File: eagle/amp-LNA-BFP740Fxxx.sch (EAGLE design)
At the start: 22 parts, among them J1 142-0701-851, J2 142-0701-851, Q1 PMOS, Q2 BFP740F

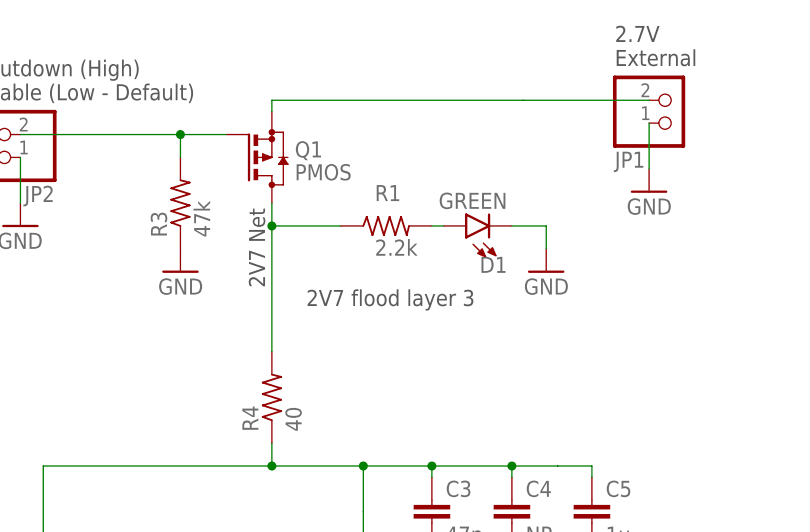
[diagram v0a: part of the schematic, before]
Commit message: BFP740F update value
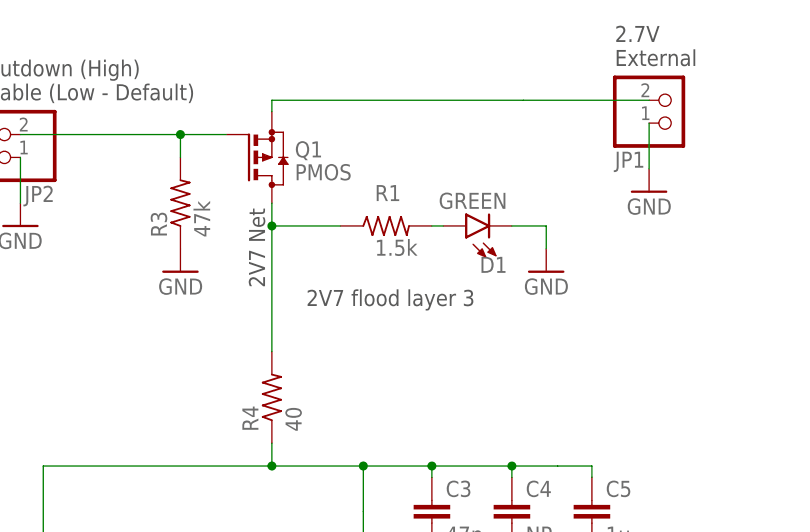
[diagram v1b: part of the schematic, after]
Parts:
- R1: value 2.2k -> 1.5k
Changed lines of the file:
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@@
 </part>
 <part name="GND80" library="supply1" deviceset="GND" device=""/>
-<part name="R1" library="oresat-rcl" deviceset="R-US_" device="0603-B-NOSILK" value="2.2k"/>
+<part name="R1" library="oresat-rcl" deviceset="R-US_" device="0603-B-NOSILK" value="1.5k"/>
 <part name="J1" library="J-Cinch-142-0701-851-SMA-end-launch" deviceset="142-0701-851" device=""/>
 <part name="J2" library="J-Cinch-142-0701-851-SMA-end-launch" deviceset="142-0701-851" device=""/>

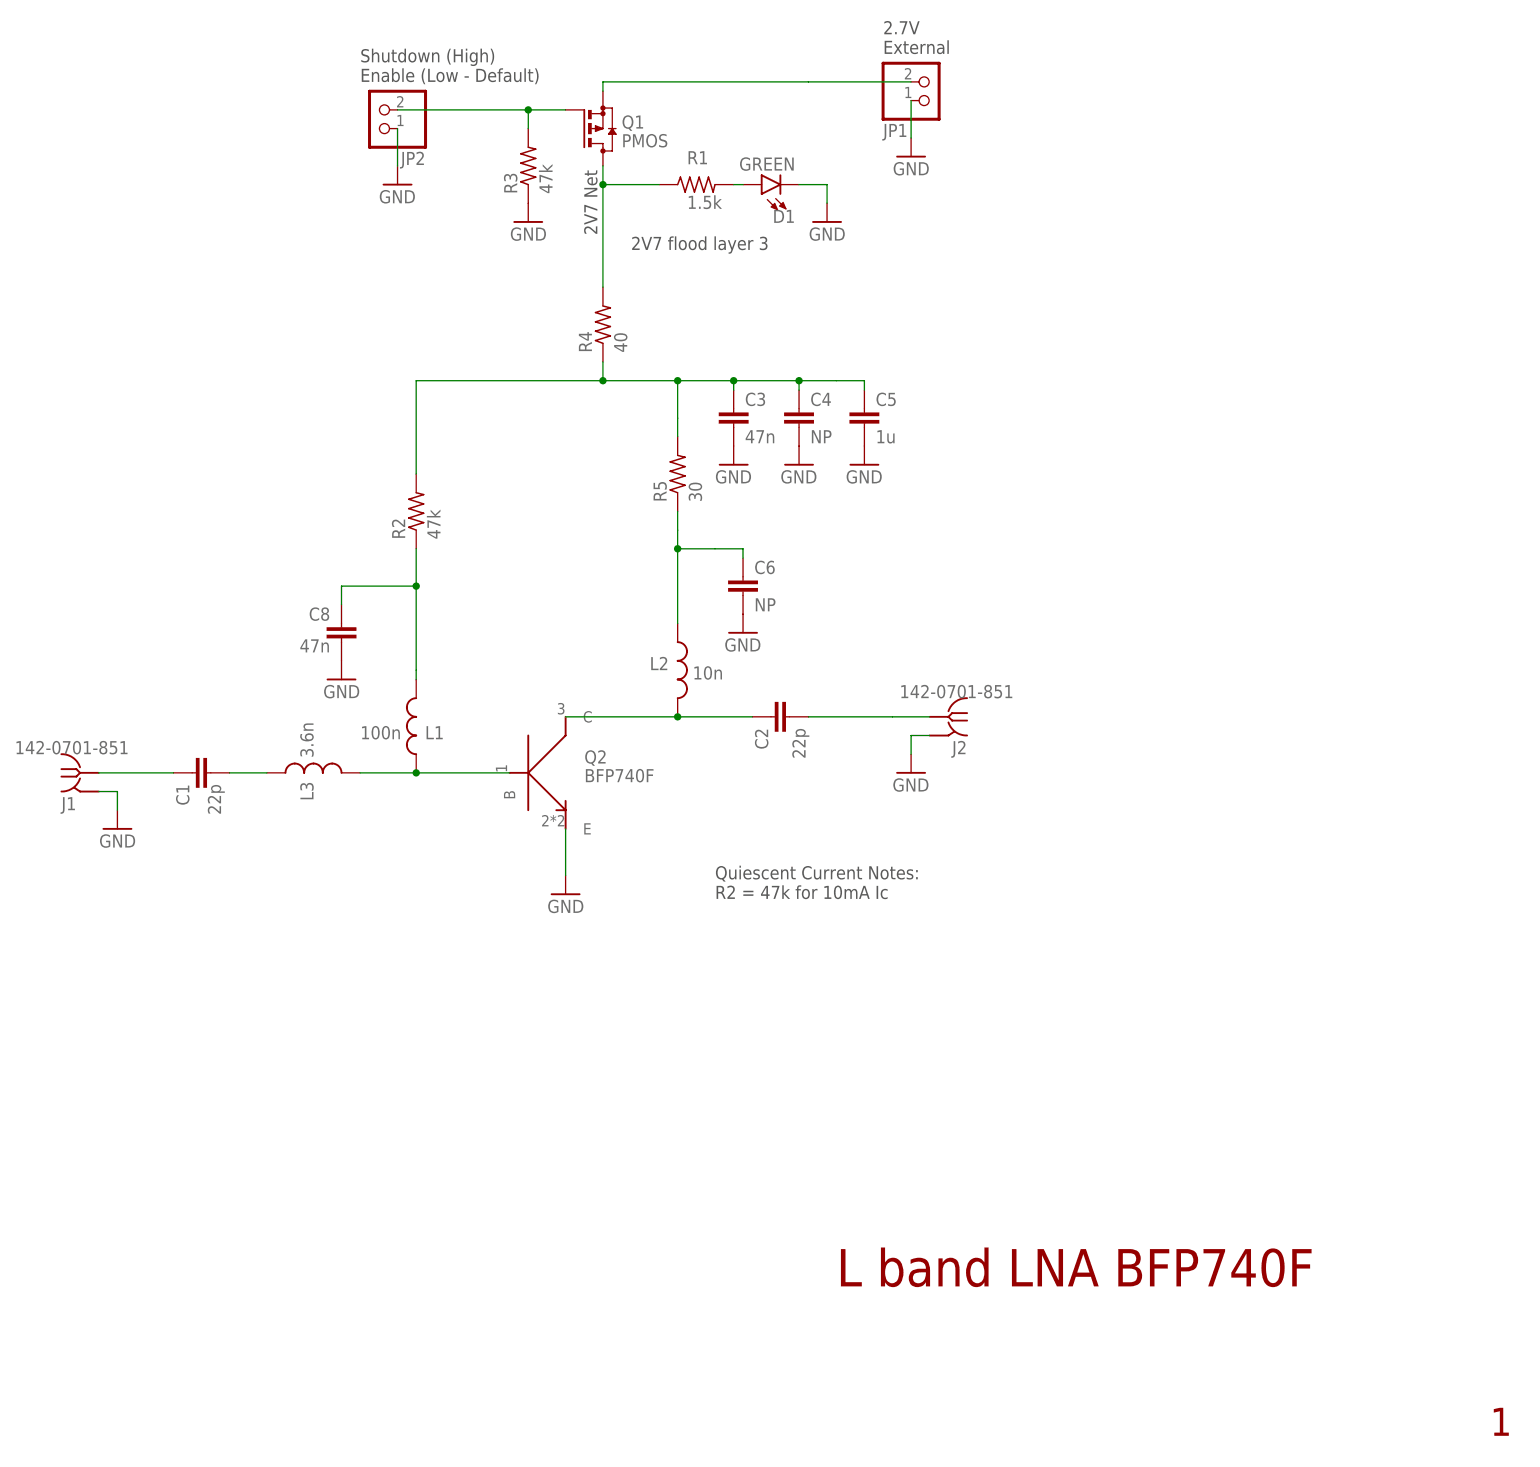
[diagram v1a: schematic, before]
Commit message: Add initial layout for LNA BFP740F
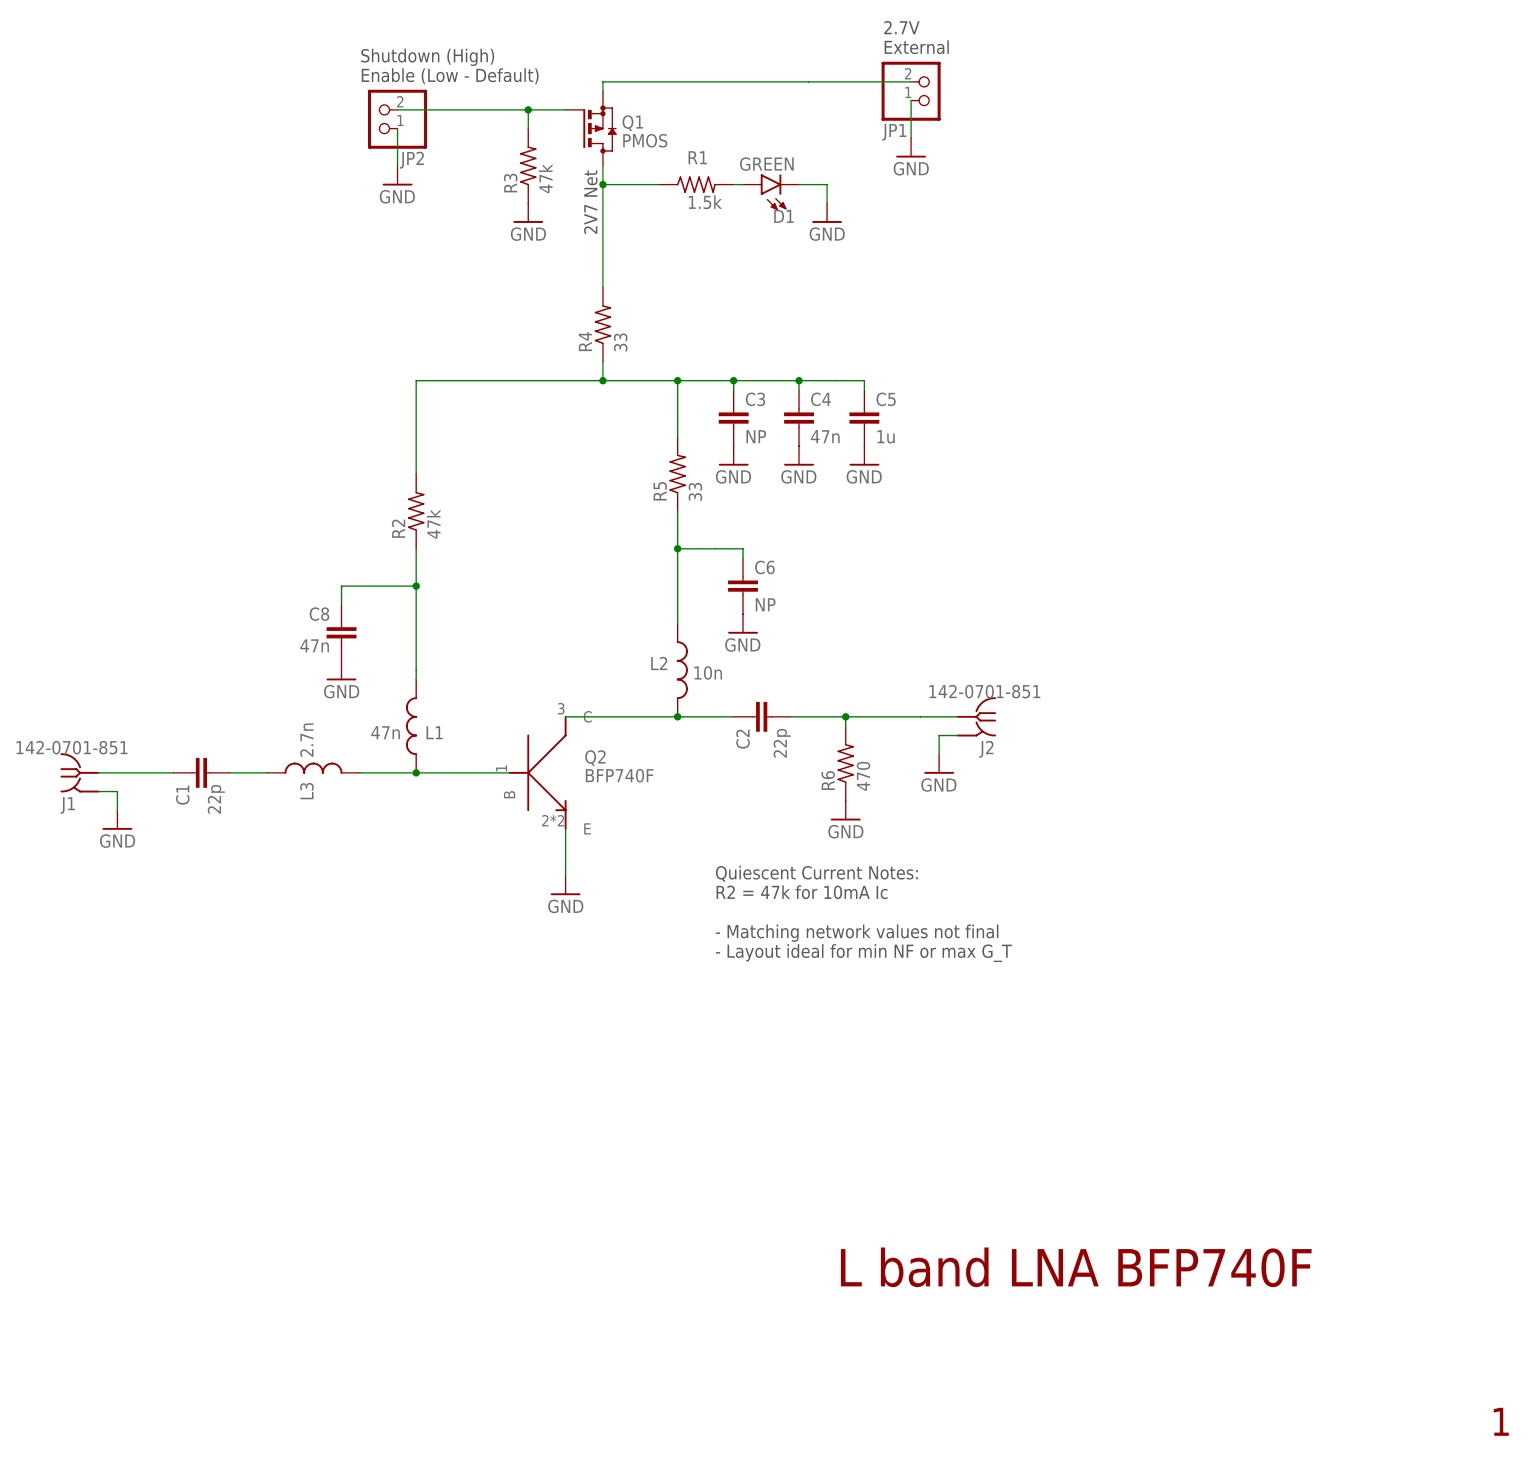
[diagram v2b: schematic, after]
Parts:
- added R6: 470, oresat-rcl:R-US_0603-C-NOSILK
- C3: value 47n -> NP; device oresat-rcl:C-EU0603-B-NOSILK -> oresat-rcl:C-EU0603-C-NOSILK
- C4: value NP -> 47n; device oresat-rcl:C-EU0603-B-NOSILK -> oresat-rcl:C-EU0603-C-NOSILK
- C5, C8: device oresat-rcl:C-EU0603-B-NOSILK -> oresat-rcl:C-EU0603-C-NOSILK
- C6: device oresat-rcl:C-EU0402-C-NOSILK -> oresat-rcl:C-EU0402-B-NOSILK
- L1: value 100n -> 47n
- L2: device oresat-rcl:L-US0402-C-NOSILK -> oresat-rcl:L-US0603-C-NOSILK
- L3: value 3.6n -> 2.7n
- R1, R2: device oresat-rcl:R-US_0603-B-NOSILK -> oresat-rcl:R-US_0603-C-NOSILK
- R4: value 40 -> 33; device oresat-rcl:R-US_0603-B-NOSILK -> oresat-rcl:R-US_0603-C-NOSILK
- R5: value 30 -> 33; device oresat-rcl:R-US_0603-B-NOSILK -> oresat-rcl:R-US_0603-C-NOSILK
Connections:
- net N$11 renamed B
- net N$4 renamed C
- net RF-IN renamed RF_IN
- removed net N$5: Q1.D, R1.1, R4.2
- new net CAPS: C3.1, C4.1, C5.1, R2.2, R4.1, R5.2
- net 2V7: now also Q1.D, R1.1, R4.2; no longer C3.1, C4.1, C5.1, R2.2, R4.1, R5.2
- net GND: now also R6.1
- net RF_OUT: now also R6.2
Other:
- note added: "Quiescent Current Notes: R2 = 47k for 10mA Ic - Matching network values not final - Layout ideal for min NF or max G_T"
- note removed: "2V7 flood layer 3"
- note removed: "Quiescent Current Notes: R2 = 47k for 10mA Ic"
- moved on the sheet: C2, J2
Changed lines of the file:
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@@
 <part name="GND29" library="supply1" library_urn="urn:adsk.eagle:library:371" deviceset="GND" device=""/>
 <part name="GND30" library="supply1" library_urn="urn:adsk.eagle:library:371" deviceset="GND" device=""/>
-<part name="C5" library="oresat-rcl" deviceset="C-EU" device="0603-B-NOSILK" value="1u"/>
-<part name="C4" library="oresat-rcl" deviceset="C-EU" device="0603-B-NOSILK" value="NP"/>
-<part name="C3" library="oresat-rcl" deviceset="C-EU" device="0603-B-NOSILK" value="47n"/>
+<part name="C5" library="oresat-rcl" deviceset="C-EU" device="0603-C-NOSILK" value="1u"/>
+<part name="C4" library="oresat-rcl" deviceset="C-EU" device="0603-C-NOSILK" value="47n"/>
+<part name="C3" library="oresat-rcl" deviceset="C-EU" device="0603-C-NOSILK" value="NP"/>
 <part name="JP1" library="pinhead" library_urn="urn:adsk.eagle:library:325" deviceset="PINHD-1X2" device="" package3d_urn="urn:adsk.eagle:package:22435/2"/>
 <part name="GND4" library="supply1" library_urn="urn:adsk.eagle:library:371" deviceset="GND" device=""/>
@@
 </part>
 <part name="GND80" library="supply1" deviceset="GND" device=""/>
-<part name="R1" library="oresat-rcl" deviceset="R-US_" device="0603-B-NOSILK" value="1.5k"/>
+<part name="R1" library="oresat-rcl" deviceset="R-US_" device="0603-C-NOSILK" value="1.5k"/>
 <part name="J1" library="J-Cinch-142-0701-851-SMA-end-launch" deviceset="142-0701-851" device=""/>
 <part name="J2" library="J-Cinch-142-0701-851-SMA-end-launch" deviceset="142-0701-851" device=""/>
 <part name="C1" library="oresat-rcl" deviceset="C-EU" device="0402-C-NOSILK" value="22p"/>
-<part name="L1" library="oresat-rcl" deviceset="L-US" device="0603-C-NOSILK" value="100n"/>
+<part name="L1" library="oresat-rcl" deviceset="L-US" device="0603-C-NOSILK" value="47n"/>
 <part name="GND5" library="supply1" library_urn="urn:adsk.eagle:library:371" deviceset="GND" device=""/>
 <part name="GND7" library="supply1" library_urn="urn:adsk.eagle:library:371" deviceset="GND" device=""/>
 <part name="GND8" library="supply1" library_urn="urn:adsk.eagle:library:371" deviceset="GND" device=""/>
-<part name="C8" library="oresat-rcl" deviceset="C-EU" device="0603-B-NOSILK" value="47n"/>
+<part name="C8" library="oresat-rcl" deviceset="C-EU" device="0603-C-NOSILK" value="47n"/>
 <part name="Q1" library="transistor-small-signal" library_urn="urn:adsk.eagle:library:401" deviceset="BSS84" device="" package3d_urn="urn:adsk.eagle:package:28738/2" value="PMOS"/>
 <part name="JP2" library="pinhead" library_urn="urn:adsk.eagle:library:325" deviceset="PINHD-1X2" device="" package3d_urn="urn:adsk.eagle:package:22435/2"/>
@@
 <part name="R3" library="oresat-rcl" deviceset="R-US_" device="0402-B-NOSILK" value="47k"/>
 <part name="GND3" library="supply1" library_urn="urn:adsk.eagle:library:371" deviceset="GND" device=""/>
-<part name="R5" library="oresat-rcl" deviceset="R-US_" device="0603-B-NOSILK" value="30"/>
+<part name="R5" library="oresat-rcl" deviceset="R-US_" device="0603-C-NOSILK" value="33"/>
 <part name="GND2" library="supply1" library_urn="urn:adsk.eagle:library:371" deviceset="GND" device=""/>
 <part name="Q2" library="Q-Infineon-BFPXXX-RF-BJT" deviceset="BFPXXXF" device="" value="BFP740F"/>
-<part name="C6" library="oresat-rcl" deviceset="C-EU" device="0402-C-NOSILK" value="NP"/>
+<part name="C6" library="oresat-rcl" deviceset="C-EU" device="0402-B-NOSILK" value="NP"/>
 <part name="GND6" library="supply1" library_urn="urn:adsk.eagle:library:371" deviceset="GND" device=""/>
-<part name="R2" library="oresat-rcl" deviceset="R-US_" device="0603-B-NOSILK" value="47k"/>
-<part name="L3" library="oresat-rcl" deviceset="L-US" device="0402-C-NOSILK" value="3.6n"/>
-<part name="R4" library="oresat-rcl" deviceset="R-US_" device="0603-B-NOSILK" value="40"/>
-<part name="L2" library="oresat-rcl" deviceset="L-US" device="0402-C-NOSILK" value="10n"/>
+<part name="R2" library="oresat-rcl" deviceset="R-US_" device="0603-C-NOSILK" value="47k"/>
+<part name="L3" library="oresat-rcl" deviceset="L-US" device="0402-C-NOSILK" value="2.7n"/>
+<part name="R4" library="oresat-rcl" deviceset="R-US_" device="0603-C-NOSILK" value="33"/>
+<part name="L2" library="oresat-rcl" deviceset="L-US" device="0603-C-NOSILK" value="10n"/>
+<part name="GND9" library="supply1" library_urn="urn:adsk.eagle:library:371" deviceset="GND" device=""/>
+<part name="R6" library="oresat-rcl" deviceset="R-US_" device="0603-C-NOSILK" value="470"/>
 </parts>
 <sheets>
@@
 <text x="111.76" y="190.5" size="1.778" layer="97">Shutdown (High)
 Enable (Low - Default)</text>
-<text x="148.59" y="167.64" size="1.778" layer="97">2V7 flood layer 3</text>
 <text x="144.018" y="169.672" size="1.778" layer="97" rot="R90">2V7 Net</text>
 <text x="160.02" y="83.82" size="1.778" layer="97" align="top-left">Quiescent Current Notes:
-R2 = 47k for 10mA Ic</text>
+R2 = 47k for 10mA Ic
+- Matching network values not final
+- Layout ideal for min NF or max G_T</text>
 </plain>
 <instances>
@@
 <attribute name="VALUE" x="142.24" y="77.47" size="1.778" layer="96" rot="MR0"/>
 </instance>
-<instance part="C2" gate="CE" x="167.64" y="104.14" smashed="yes" rot="MR270">
-<attribute name="NAME" x="167.259" y="102.616" size="1.778" layer="95" rot="MR270"/>
-<attribute name="VALUE" x="172.339" y="102.616" size="1.778" layer="96" rot="MR270"/>
-</instance>
-<instance part="GND29" gate="1" x="186.69" y="96.52" smashed="yes">
-<attribute name="VALUE" x="184.15" y="93.98" size="1.778" layer="96"/>
+<instance part="C2" gate="CE" x="165.1" y="104.14" smashed="yes" rot="MR270">
+<attribute name="NAME" x="164.719" y="102.616" size="1.778" layer="95" rot="MR270"/>
+<attribute name="VALUE" x="169.799" y="102.616" size="1.778" layer="96" rot="MR270"/>
+</instance>
+<instance part="GND29" gate="1" x="190.5" y="96.52" smashed="yes">
+<attribute name="VALUE" x="187.96" y="93.98" size="1.778" layer="96"/>
 </instance>
 <instance part="GND30" gate="1" x="78.74" y="88.9" smashed="yes" rot="MR0">
@@
 <attribute name="VALUE" x="64.77" y="99.06" size="1.778" layer="96"/>
 </instance>
-<instance part="J2" gate="G$1" x="191.77" y="104.14" smashed="yes" rot="MR0">
-<attribute name="NAME" x="194.31" y="99.06" size="1.778" layer="95" rot="MR0"/>
-<attribute name="VALUE" x="200.66" y="106.68" size="1.778" layer="96" rot="MR0"/>
+<instance part="J2" gate="G$1" x="195.58" y="104.14" smashed="yes" rot="MR0">
+<attribute name="NAME" x="198.12" y="99.06" size="1.778" layer="95" rot="MR0"/>
+<attribute name="VALUE" x="204.47" y="106.68" size="1.778" layer="96" rot="MR0"/>
 </instance>
 <instance part="C1" gate="CE" x="88.9" y="96.52" smashed="yes" rot="MR270">
@@
 <attribute name="NAME" x="151.13" y="110.49" size="1.778" layer="95"/>
 <attribute name="VALUE" x="156.972" y="109.22" size="1.778" layer="96"/>
+</instance>
+<instance part="GND9" gate="1" x="177.8" y="90.17" smashed="yes" rot="MR0">
+<attribute name="VALUE" x="180.34" y="87.63" size="1.778" layer="96" rot="MR0"/>
+</instance>
+<instance part="R6" gate="R" x="177.8" y="97.79" smashed="yes" rot="R90">
+<attribute name="NAME" x="176.3014" y="93.98" size="1.778" layer="95" rot="R90"/>
+<attribute name="VALUE" x="181.102" y="93.98" size="1.778" layer="96" rot="R90"/>
 </instance>
 </instances>
@@
 <net name="GND" class="0">
 <segment>
-<wire x1="186.69" y1="101.6" x2="189.23" y2="101.6" width="0.1524" layer="91"/>
+<wire x1="190.5" y1="101.6" x2="193.04" y2="101.6" width="0.1524" layer="91"/>
 <pinref part="GND29" gate="1" pin="GND"/>
-<wire x1="186.69" y1="99.06" x2="186.69" y2="101.6" width="0.1524" layer="91"/>
+<wire x1="190.5" y1="99.06" x2="190.5" y2="101.6" width="0.1524" layer="91"/>
 <pinref part="J2" gate="G$1" pin="GND"/>
 </segment>
@@
 <pinref part="GND6" gate="1" pin="GND"/>
 </segment>
-</net>
-<net name="RF_OUT" class="2">
-<segment>
-<wire x1="184.15" y1="104.14" x2="189.23" y2="104.14" width="0.1524" layer="91"/>
+<segment>
+<pinref part="GND9" gate="1" pin="GND"/>
+<pinref part="R6" gate="R" pin="1"/>
+</segment>
+</net>
+<net name="RF_OUT" class="0">
+<segment>
+<wire x1="187.96" y1="104.14" x2="193.04" y2="104.14" width="0.1524" layer="91"/>
 <pinref part="C2" gate="CE" pin="2"/>
-<wire x1="184.15" y1="104.14" x2="172.72" y2="104.14" width="0.1524" layer="91"/>
+<wire x1="187.96" y1="104.14" x2="177.8" y2="104.14" width="0.1524" layer="91"/>
 <pinref part="J2" gate="G$1" pin="RF"/>
+<wire x1="177.8" y1="104.14" x2="170.18" y2="104.14" width="0.1524" layer="91"/>
+<wire x1="177.8" y1="102.87" x2="177.8" y2="104.14" width="0.1524" layer="91"/>
+<junction x="177.8" y="104.14"/>
+<pinref part="R6" gate="R" pin="2"/>
 </segment>
 </net>
@@
 </segment>
 </net>
-<net name="2V7" class="0">
+<net name="CAPS" class="0">
 <segment>
 <wire x1="144.78" y1="149.86" x2="154.94" y2="149.86" width="0.1524" layer="91"/>
@@
 </segment>
 </net>
-<net name="N$4" class="1">
+<net name="C" class="0">
 <segment>
 <pinref part="C2" gate="CE" pin="1"/>
-<wire x1="165.1" y1="104.14" x2="154.94" y2="104.14" width="0.1524" layer="91"/>
+<wire x1="162.56" y1="104.14" x2="154.94" y2="104.14" width="0.1524" layer="91"/>
 <pinref part="Q2" gate="G$1" pin="C"/>
 <wire x1="139.7" y1="104.14" x2="154.94" y2="104.14" width="0.1524" layer="91"/>
@@
 </segment>
 </net>
-<net name="N$11" class="1">
+<net name="B" class="0">
 <segment>
 <pinref part="L1" gate="L" pin="1"/>
@@
 </segment>
 </net>
-<net name="RF-IN" class="2">
+<net name="RF_IN" class="0">
 <segment>
 <pinref part="J1" gate="G$1" pin="RF"/>
@@
 </segment>
 </net>
-<net name="N$5" class="0">
+<net name="2V7" class="0">
 <segment>
 <pinref part="Q1" gate="G$1" pin="D"/>
